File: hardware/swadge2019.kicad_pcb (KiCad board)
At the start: 2 copper layers, 100 x 95.3 mm, 50 parts, among them P1 PGM, P10 CONN_1, P11 CONN_1, P12 CONN_1, P13 CONN_1, P2 USBMicroB-10118192-0001LF, P3 SAO, P7 CONN_1, P8 CONN_1, P9 CONN_1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

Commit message: Add RevD
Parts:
- removed the G*** at (76.2, 105.8)
- removed the G*** at (76.2, 105.7)
- added G*** (x2): LOGO, LOGO, B.Cu at (76.3, 111.4)
- C2: value 1u -> .22u
- C4, C5, C6, C7, C8: value .1u -> .22u
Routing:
- net +5V: track 84.7 -> 127.9 mm, vias 2 -> 3
- net Net-(SW7-Pad3): track 66.3 -> 104.7 mm
- net GND: track 223.3 -> 226.5 mm
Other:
- board text added: "SWADGE2019 REV D All Aircraft Report"
- board text removed: "SWADGE2019 REV C All Aircraft Report"

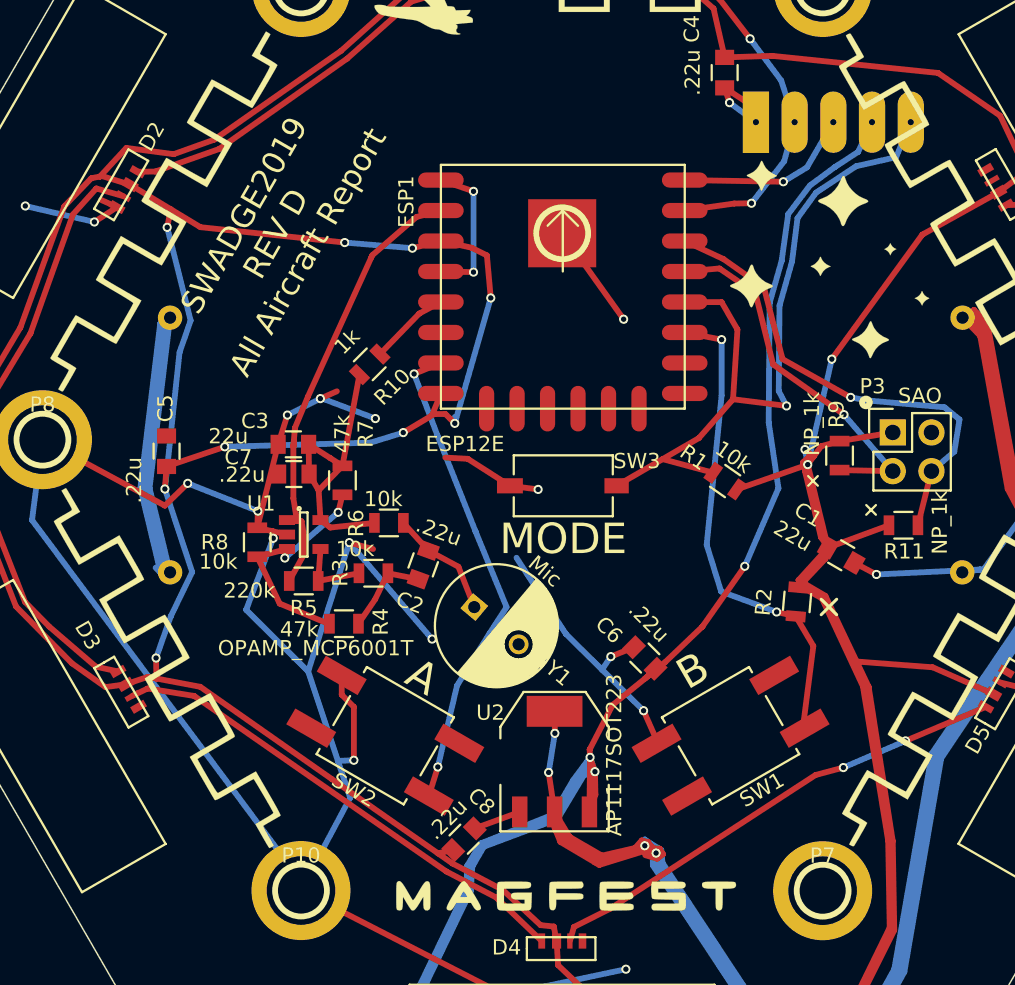
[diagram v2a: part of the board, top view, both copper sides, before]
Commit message: Moving Microphone around + removing holes for programming pins.
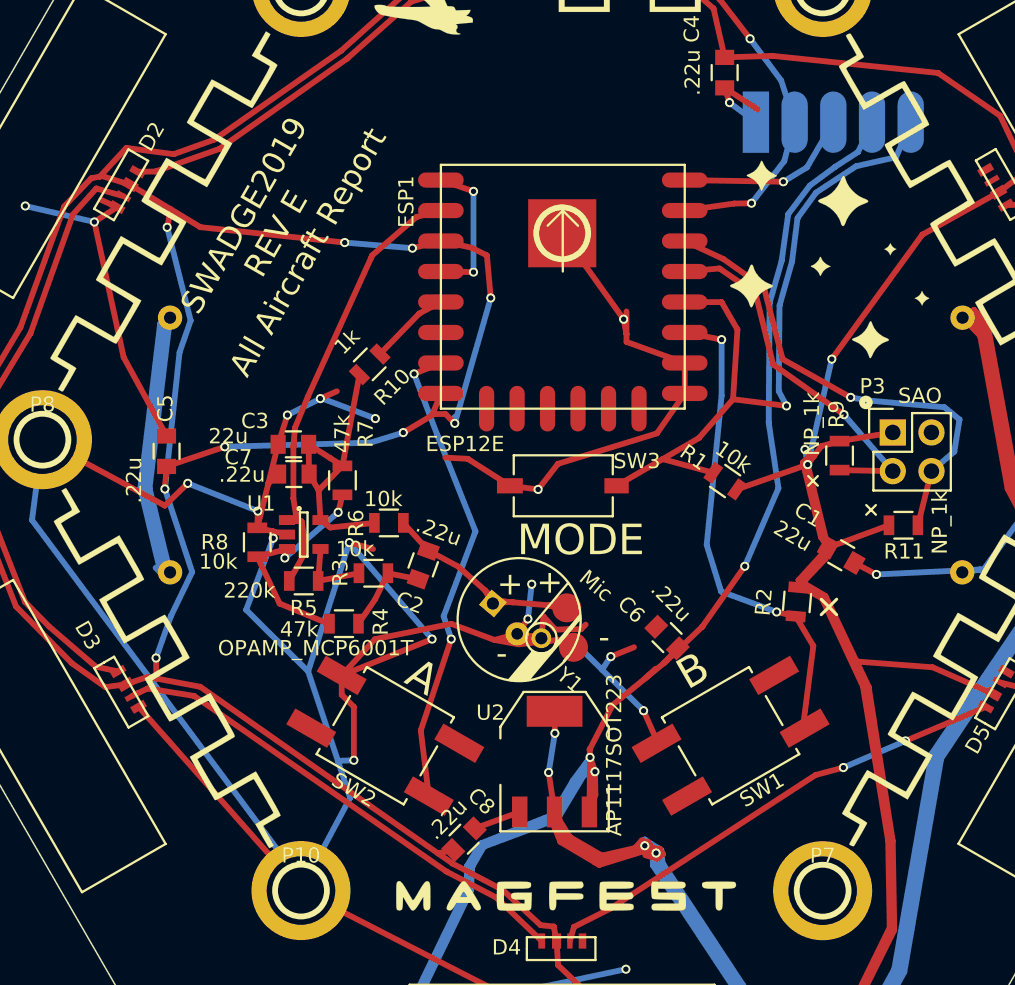
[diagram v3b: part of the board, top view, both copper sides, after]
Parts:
- moved C6 1.98 mm to (83.1, 89.2)
- moved Y1 1.54 mm to (71.9, 86.8)
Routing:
- net GND: track 226.5 -> 313.5 mm, vias 19 -> 21
- net Net-(C2-Pad2): track 7.53 -> 17.6 mm
- net +5V: track 127.9 -> 129.2 mm
- net GPIO13: track 31.9 -> 31.2 mm
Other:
- board text added: "SWADGE2019 REV E All Aircraft Report"
- board text removed: "SWADGE2019 REV D All Aircraft Report"

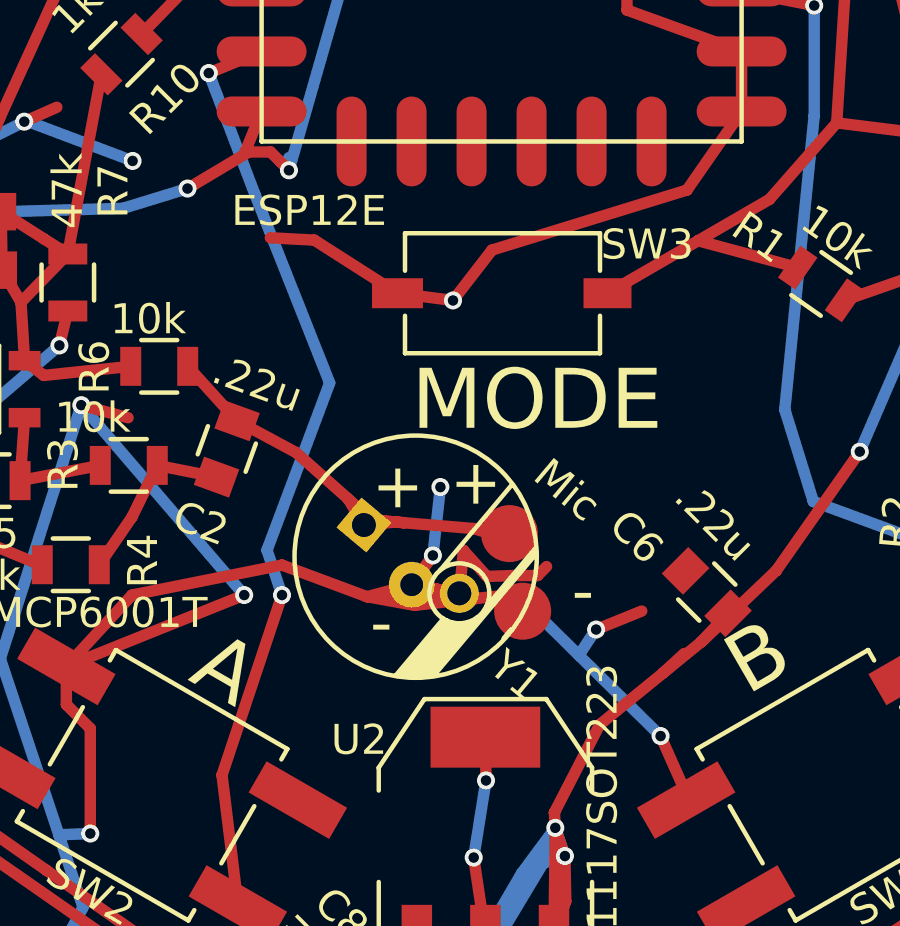
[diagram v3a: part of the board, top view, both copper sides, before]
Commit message: Update rev with better microphone support
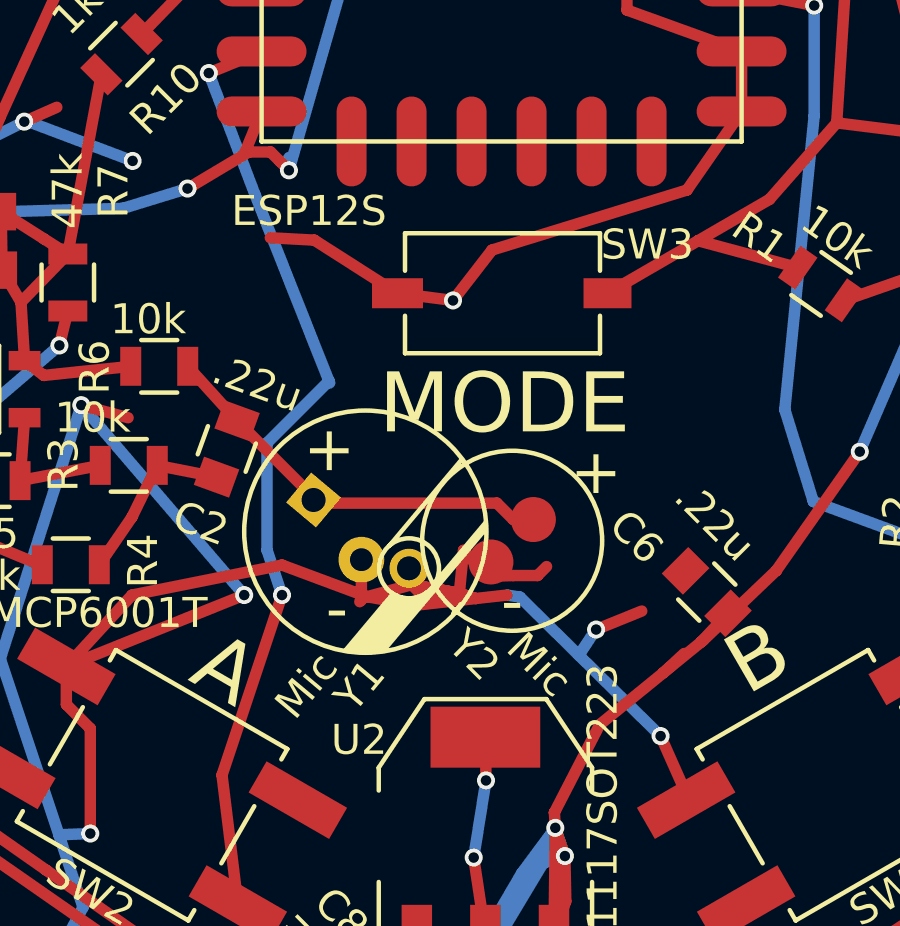
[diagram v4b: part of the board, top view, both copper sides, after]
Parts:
- added Y2: Mic, 6mmELECTRET_MIC_SMT, F.Cu at (76.6, 87.5)
- ESP1: value ESP12E -> ESP12S
- moved Y1 1.87 mm to (70.3, 86.0)
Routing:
- net Net-(C2-Pad2): track 17.6 -> 13.7 mm
- net GND: track 313.5 -> 311.4 mm, vias 21 -> 19
- net GPIO13: track 31.2 -> 31.7 mm
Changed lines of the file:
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@@
     (area 17.593375 24.188475 134.806625 132.340001)
     (thickness 1.6)
-    (drawings 152)
-    (tracks 606)
+    (drawings 153)
+    (tracks 598)
     (zones 0)
-    (modules 50)
+    (modules 51)
     (nets 27)
   )
@@
   )
   (module C_Radial_D8_L13_P3.8 (layer F.Cu)
-    (at 71.93 86.83 320)
+    (at 70.252 85.996 320)
     (descr "Radial Electrolytic Capacitor Diameter 8mm x Length 13mm, Pitch 3.8mm")
     (tags "Electrolytic Capacitor")
-    (fp_text reference Y1 (at 7 0.9 320) (layer F.SilkS)
+    (fp_text reference Y1 (at 5.054578 4.048042 410) (layer F.SilkS)
       (effects (font (size 1 1) (thickness 0.15)))
     )
-    (fp_text value Mic (at 4.336501 -4.944164 500) (layer F.SilkS)
+    (fp_text value Mic (at 3.692551 5.190918 590) (layer F.SilkS)
       (effects (font (size 1 1) (thickness 0.15)))
     )
@@
     (pad 2 thru_hole circle (at 2.4 0.8 320) (size 1.524 1.524) (drill 0.762) (layers *.Cu *.Mask F.SilkS)
       (net 2 GND))
-    (pad 1 smd circle (at 3.8 -2.6 320) (size 1.9 1.9) (layers F.Cu F.Paste F.Mask)
-      (net 4 "Net-(C2-Pad2)"))
-    (pad 2 smd circle (at 5.8 -0.9 320) (size 1.9 1.9) (layers F.Cu F.Paste F.Mask)
-      (net 2 GND))
   )
   (module LOGO (layer B.Cu)
@@
       (effects (font (size 1 1) (thickness 0.15)))
     )
-    (fp_text value ESP12E (at -6.42 14.32) (layer F.SilkS)
+    (fp_text value ESP12S (at -6.42 14.32) (layer F.SilkS)
       (effects (font (size 1 1) (thickness 0.15)))
     )
@@
       (effects (font (size 1 1) (thickness 0.15)))
     )
-    (fp_text value MODE (at -1.15 -3.56 180) (layer F.SilkS)
+    (fp_text value MODE (at -0.068 -3.678 180) (layer F.SilkS)
       (effects (font (size 2 2) (thickness 0.3)))
     )
@@
     )
   )
-  (gr_text - (at 72.24 90.53 180) (layer F.SilkS)
+  (module 6mmELECTRET_MIC_SMT (layer F.Cu)
+    (at 76.602 87.52 225)
+    (fp_text reference Y2 (at 3.592102 -1.796051 315) (layer F.SilkS)
+      (effects (font (size 1 1) (thickness 0.15)))
+    )
+    (fp_text value Mic (at 2.286 -3.556 315) (layer F.SilkS)
+      (effects (font (size 1 1) (thickness 0.15)))
+    )
+    (fp_circle (center 0 0) (end 3 0) (layer F.SilkS) (width 0.15))
+    (pad 1 smd circle (at -1 0 225) (size 1.5 1.5) (layers F.Cu F.Paste F.Mask)
+      (net 4 "Net-(C2-Pad2)"))
+    (pad 2 smd circle (at 1 0 225) (size 1.5 1.5) (layers F.Cu F.Paste F.Mask)
+      (net 2 GND))
+  )
+  (gr_text - (at 76.602 89.806 180) (layer F.SilkS)
     (effects (font (size 1.5 1.5) (thickness 0.3)))
   )
-  (gr_text + (at 75.39 85.59) (layer F.SilkS)
+  (gr_text + (at 79.396 85.234) (layer F.SilkS)
     (effects (font (size 1.5 1.5) (thickness 0.3)))
   )
-  (gr_text - (at 78.96 89.47 180) (layer F.SilkS)
+  (gr_text - (at 72.24 90.53 180) (layer F.SilkS)
+    (effects (font (size 1.5 1.5) (thickness 0.3)))
+  )
+  (gr_text - (at 70.76 90.06 180) (layer F.SilkS)
     (effects (font (size 1.5 1.5) (thickness 0.3)))
   )
-  (gr_text + (at 72.79 85.71) (layer F.SilkS)
+  (gr_text + (at 70.506 84.472) (layer F.SilkS)
     (effects (font (size 1.5 1.5) (thickness 0.3)))
   )
@@
   (segment (start 52.47 62.3) (end 50.49 61.103588) (width 0.381) (layer F.Cu) (net 1))
   (via (at 61.94 63.31) (size 0.6) (drill 0.35) (layers F.Cu B.Cu) (net 1))
+  (segment (start 71.576277 88.151526) (end 71.576277 89.497723) (width 0.381) (layer F.Cu) (net 2))
+  (segment (start 71.576277 89.497723) (end 71.522 89.552) (width 0.381) (layer F.Cu) (net 2))
   (segment (start 76.63 88.68) (end 77.45 88.68) (width 0.381) (layer F.Cu) (net 2))
   (segment (start 75.76 88.71) (end 76.63 88.68) (width 0.381) (layer F.Cu) (net 2))
@@
   (segment (start 74.840969 89.272593) (end 74.98 87.84) (width 0.381) (layer F.Cu) (net 2))
   (segment (start 77.45 88.68) (end 77.75 88.38) (width 0.381) (layer F.Cu) (net 2))
-  (segment (start 74.840969 89.272593) (end 73.541344 89.272593) (width 0.381) (layer F.Cu) (net 2) (status C00000))
-  (segment (start 73.541344 89.272593) (end 73.254277 88.985526) (width 0.381) (layer F.Cu) (net 2) (status C00000))
+  (segment (start 74.840969 89.272593) (end 73.541344 89.272593) (width 0.381) (layer F.Cu) (net 2))
+  (segment (start 73.541344 89.272593) (end 73.254277 88.985526) (width 0.381) (layer F.Cu) (net 2))
   (segment (start 74.840969 89.272593) (end 75.386944 89.446057) (width 0.381) (layer F.Cu) (net 2))
   (segment (start 75.386944 89.446057) (end 74.840969 89.272593) (width 0.381) (layer F.Cu) (net 2))
   (segment (start 73.254277 88.985526) (end 74.840969 89.272593) (width 0.381) (layer F.Cu) (net 2))
   (segment (start 73.254277 88.985526) (end 74.840969 89.272593) (width 0.381) (layer F.Cu) (net 2))
-  (segment (start 73.254277 88.985526) (end 73.96 88.01) (width 0.381) (layer F.Cu) (net 2))
-  (via (at 73.96 88.01) (size 0.6) (drill 0.35) (layers F.Cu B.Cu) (net 2))
-  (segment (start 73.96 88.01) (end 74.21 85.73) (width 0.381) (layer B.Cu) (net 2))
-  (via (at 74.21 85.73) (size 0.6) (drill 0.35) (layers F.Cu B.Cu) (net 2))
-  (segment (start 74.21 85.73) (end 74.18 85.73) (width 0.381) (layer F.Cu) (net 2))
   (segment (start 80.24 68.34) (end 80.43 69.33) (width 0.381) (layer F.Cu) (net 2))
   (segment (start 84.25 71.21) (end 80.43 69.83) (width 0.381) (layer F.Cu) (net 2))
@@
   (segment (start 63.93 86.73) (end 64.772 85.008) (width 0.381) (layer F.Cu) (net 3))
   (segment (start 64.772 85.008) (end 66.74798 85.399693) (width 0.381) (layer F.Cu) (net 3))
-  (segment (start 72.698188 86.896386) (end 71.759708 86.896386) (width 0.381) (layer F.Cu) (net 4) (status 800000))
-  (segment (start 71.759708 86.896386) (end 71.660559 86.995535) (width 0.381) (layer F.Cu) (net 4) (status C00000))
-  (segment (start 71.660559 86.995535) (end 71.130601 86.119072) (width 0.381) (layer F.Cu) (net 4))
-  (segment (start 72.71 86.895257) (end 72.698188 86.896386) (width 0.381) (layer F.Cu) (net 4))
-  (segment (start 72.698188 86.896386) (end 71.660559 86.995535) (width 0.381) (layer F.Cu) (net 4))
-  (segment (start 75.31147 87.112904) (end 76.383659 87.434086) (width 0.381) (layer F.Cu) (net 4))
-  (segment (start 72.99 86.918683) (end 72.71 86.895257) (width 0.381) (layer F.Cu) (net 4))
-  (segment (start 72.71 86.895257) (end 71.93 86.83) (width 0.381) (layer F.Cu) (net 4))
-  (segment (start 76.077241 87.176971) (end 75.31147 87.112904) (width 0.381) (layer F.Cu) (net 4))
-  (segment (start 75.31147 87.112904) (end 72.99 86.918683) (width 0.381) (layer F.Cu) (net 4))
-  (segment (start 72.99 86.918683) (end 71.93 86.83) (width 0.381) (layer F.Cu) (net 4))
-  (segment (start 71.93 86.83) (end 71.130601 86.119072) (width 0.381) (layer F.Cu) (net 4))
-  (segment (start 71.130601 86.119072) (end 69.4 84.58) (width 0.381) (layer F.Cu) (net 4))
-  (segment (start 69.4 84.58) (end 67.43202 83.520307) (width 0.381) (layer F.Cu) (net 4))
+  (segment (start 77.309107 86.812893) (end 76.640893 86.812893) (width 0.381) (layer F.Cu) (net 4) (status C00000))
+  (segment (start 76.640893 86.812893) (end 76.094 86.266) (width 0.381) (layer F.Cu) (net 4) (status 400000))
+  (segment (start 76.094 86.266) (end 70.087024 86.266) (width 0.381) (layer F.Cu) (net 4))
+  (segment (start 70.087024 86.266) (end 69.982559 86.161535) (width 0.381) (layer F.Cu) (net 4))
+  (segment (start 69.982559 86.161535) (end 69.982559 86.070846) (width 0.381) (layer F.Cu) (net 4))
+  (segment (start 69.982559 86.070846) (end 67.43202 83.520307) (width 0.381) (layer F.Cu) (net 4))
   (segment (start 67.43202 83.520307) (end 65.788 81.706) (width 0.381) (layer F.Cu) (net 4))
   (segment (start 59.6 78.5) (end 59.57 76.55) (width 0.381) (layer F.Cu) (net 5))
@@
   (segment (start 50.48 84.95) (end 49.13 79.43) (width 0.381) (layer B.Cu) (net 23))
   (segment (start 49.13 79.43) (end 50.48 68.24) (width 0.381) (layer B.Cu) (net 23))
-  (segment (start 67.458143 99.629551) (end 66.93 95.33) (width 0.381) (layer F.Cu) (net 24))
-  (segment (start 66.93 95.33) (end 68.93 89.33) (width 0.381) (layer F.Cu) (net 24))
-  (via (at 68.93 89.33) (size 0.6) (drill 0.35) (layers F.Cu B.Cu) (net 24))
+  (segment (start 68.43 87.83) (end 68.43 84.262) (width 0.381) (layer B.Cu) (net 24))
   (segment (start 68.93 89.33) (end 68.43 87.83) (width 0.381) (layer B.Cu) (net 24))
-  (segment (start 68.43 87.83) (end 70.52 82.26) (width 0.381) (layer B.Cu) (net 24))
-  (segment (start 68.03 75.98) (end 70.52 82.26) (width 0.381) (layer B.Cu) (net 24))
+  (via (at 68.93 89.33) (size 0.6) (drill 0.35) (layers F.Cu B.Cu) (net 24))
+  (segment (start 66.93 95.33) (end 68.93 89.33) (width 0.381) (layer F.Cu) (net 24))
+  (segment (start 67.458143 99.629551) (end 66.93 95.33) (width 0.381) (layer F.Cu) (net 24))
+  (segment (start 70.495015 82.196985) (end 70.495015 82.196986) (width 0.381) (layer B.Cu) (net 24))
+  (segment (start 68.43 84.262) (end 70.495015 82.196985) (width 0.381) (layer B.Cu) (net 24))
+  (segment (start 68.03 75.98) (end 70.495015 82.196986) (width 0.381) (layer B.Cu) (net 24))
+  (segment (start 70.495015 82.196986) (end 70.52 82.26) (width 0.381) (layer B.Cu) (net 24))
   (segment (start 66.49 71.93) (end 68.03 75.98) (width 0.381) (layer B.Cu) (net 24))
   (segment (start 68.25 71.21) (end 66.49 71.93) (width 0.381) (layer F.Cu) (net 24))

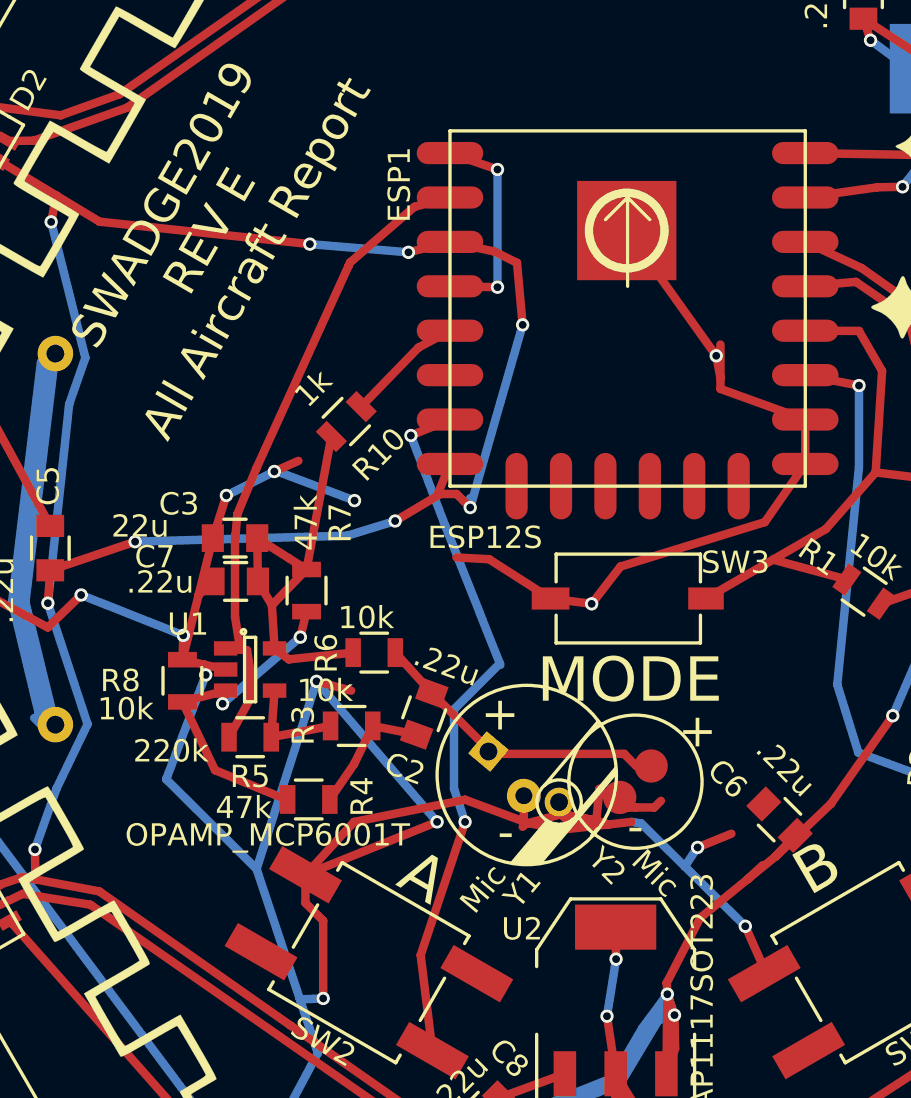
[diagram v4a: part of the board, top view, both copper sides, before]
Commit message: Bump rev G gerbers.
Remove SMT mic.

Add new holes for smaller possible mic spacing
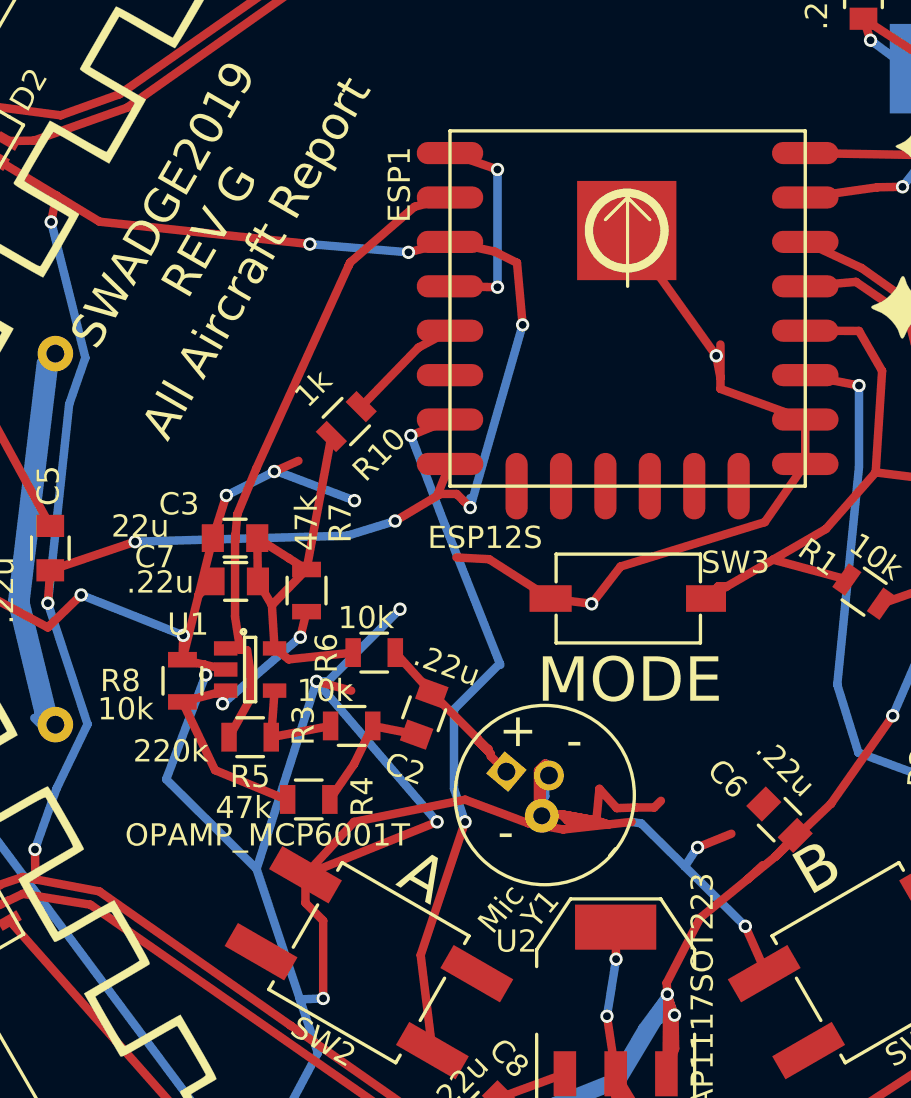
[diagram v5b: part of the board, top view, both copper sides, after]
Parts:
- removed Y2: Mic, 6mmELECTRET_MIC_SMT
- moved Y1 1.21 mm to (71.1, 86.9)
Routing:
- net GND: track 311.4 -> 320.9 mm, vias 19 -> 20
- net Net-(C2-Pad2): track 13.7 -> 8.73 mm
- net GPIO0: track 48.7 -> 49.9 mm
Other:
- board text added: "SWADGE2019 REV G All Aircraft Report"
- board text removed: "SWADGE2019 REV E All Aircraft Report"
